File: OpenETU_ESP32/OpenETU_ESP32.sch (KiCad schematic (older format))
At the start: 2 parts

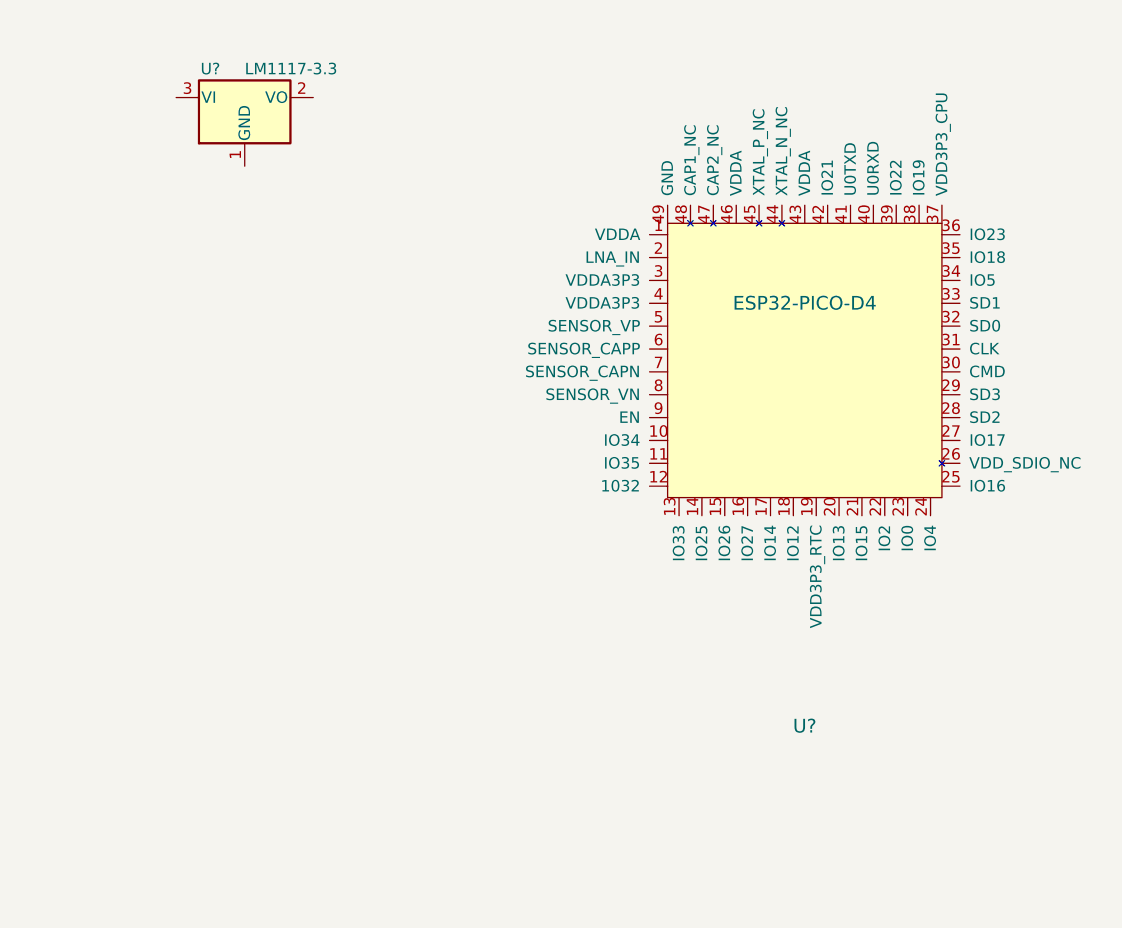
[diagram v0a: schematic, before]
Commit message: Changes
Started ramping up Schematic design for the esp32 vs of this board
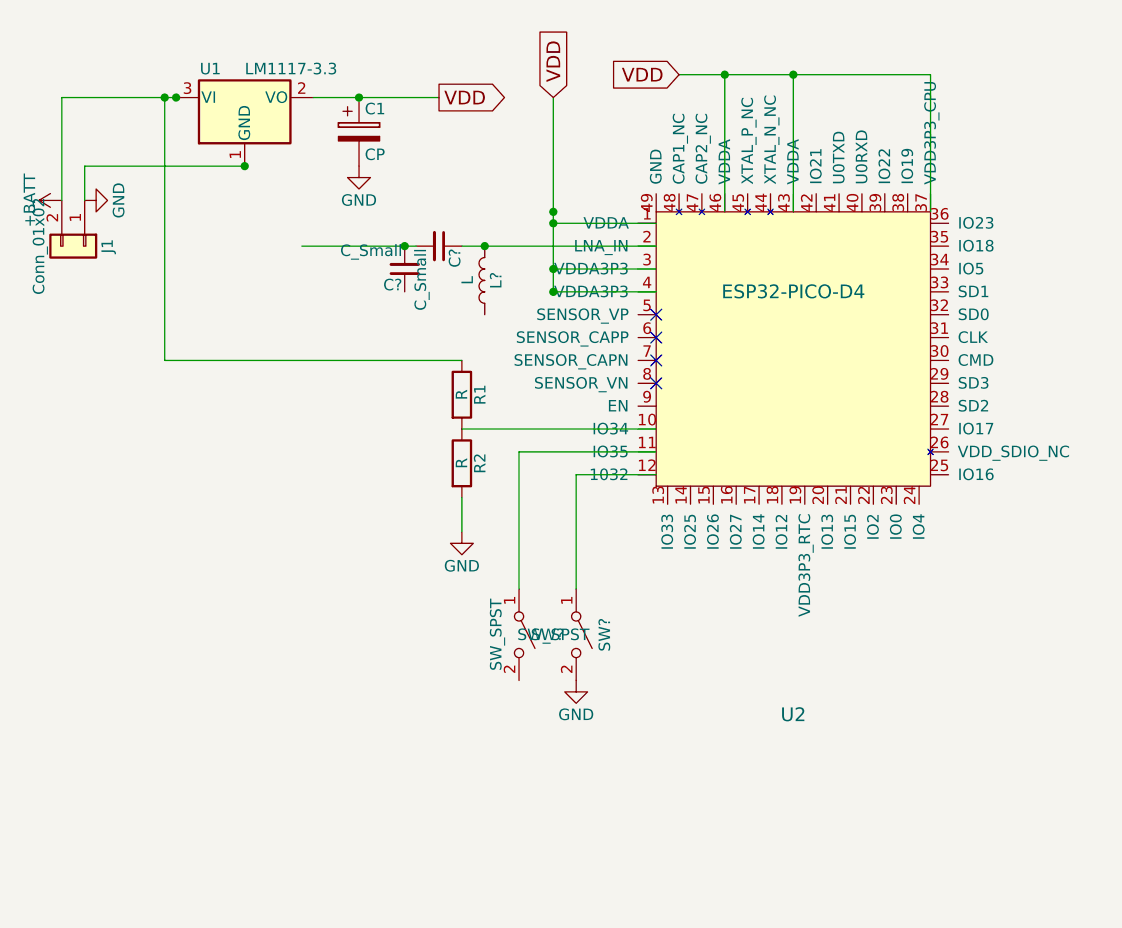
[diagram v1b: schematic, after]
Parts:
- added C1: CP, symbol CP
- added C? (x2): C_Small, symbol C_Small
- added J1: Conn_01x02, symbol Conn_01x02
- added L?: L, symbol L
- added R1, R2: R, symbol R
- added SW? (x2): SW_SPST, symbol SW_SPST
- gave numbers to parts that had none: 2
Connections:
- net labels added: +BATT, GND, VDD
- wire segments 0 -> 23
- no-connect marks 0 -> 4
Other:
- moved on the sheet: U2

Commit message: Just updating for the night
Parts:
- added C? (x2): C_Small, symbol C_Small
- added D?: LED, symbol LED
- added IC?: A1302KUA-T, symbol A1302KUA-T
- added R?: R_Small, symbol R_Small
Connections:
- wire segments 23 -> 31
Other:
- moved on the sheet: C?, L?
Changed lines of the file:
@@
 LIBS:valves
 LIBS:esp32-pico-d4
+LIBS:ETrigger-smaliffying-cache
 LIBS:OpenETU_ESP32-cache
 EELAYER 25 0
@@
 	1    0    0    -1
 $EndComp
-Wire Wire Line
-	3650 2850 4200 2850
 $Comp
 L GND #PWR01
@@
 	1    0    0    -1
 $EndComp
-Connection ~ 3850 2850
 Text GLabel 4200 2850 2    60   Output ~ 0
 VDD
-Wire Wire Line
-	5150 3400 4700 3400
-Wire Wire Line
-	4700 2850 4700 3700
-Wire Wire Line
-	4700 3700 5150 3700
-Connection ~ 4700 3400
-Wire Wire Line
-	5150 3600 4700 3600
-Connection ~ 4700 3600
 Text GLabel 4700 2850 1    60   Input ~ 0
 VDD
-Wire Wire Line
-	5450 3350 5450 2750
-Wire Wire Line
-	5250 2750 6350 2750
-Wire Wire Line
-	5750 2750 5750 3350
-Wire Wire Line
-	6350 2750 6350 3350
-Connection ~ 5750 2750
-Connection ~ 5450 2750
 Text GLabel 5250 2750 0    60   Input ~ 0
 VDD
@@
 NoConn ~ 5150 4000
 NoConn ~ 5150 4100
-Wire Wire Line
-	3050 2850 2550 2850
-Wire Wire Line
-	2550 2850 2550 3300
 $Comp
 L Conn_01x02 J1
@@
 	0    1    1    0
 $EndComp
-Wire Wire Line
-	3350 3150 2650 3150
-Wire Wire Line
-	2650 3150 2650 3300
-Connection ~ 3000 2850
 $Comp
 L R R1
@@
 	1    0    0    -1
 $EndComp
-Wire Wire Line
-	3000 2850 3000 4000
-Wire Wire Line
-	3000 4000 4300 4000
-Wire Wire Line
-	4300 4300 5150 4300
 $Comp
 L R R2
@@
 	1    0    0    -1
 $EndComp
-Wire Wire Line
-	4300 4600 4300 4750
 $Comp
 L GND #PWR02
@@
 	0    -1   -1   0
 $EndComp
-Connection ~ 3350 3150
-Connection ~ 4700 3700
-Connection ~ 4700 3350
-Connection ~ 3050 2850
-Wire Wire Line
-	4300 3500 5150 3500
 $Comp
 L L L?
 U 1 1 5A060289
-P 4400 3650
-F 0 "L?" V 4350 3650 50  0000 C CNN
-F 1 "L" V 4475 3650 50  0000 C CNN
-F 2 "" H 4400 3650 50  0001 C CNN
-F 3 "" H 4400 3650 50  0001 C CNN
-	1    4400 3650
-	-1   0    0    1
+P 4250 3500
+F 0 "L?" V 4200 3500 50  0000 C CNN
+F 1 "L" V 4325 3500 50  0000 C CNN
+F 2 "" H 4250 3500 50  0001 C CNN
+F 3 "" H 4250 3500 50  0001 C CNN
+	1    4250 3500
+	0    -1   -1   0
 $EndComp
 $Comp
 L C_Small C?
 U 1 1 5A06032C
-P 4200 3500
-F 0 "C?" H 4210 3570 50  0000 L CNN
-F 1 "C_Small" H 4210 3420 50  0000 L CNN
-F 2 "" H 4200 3500 50  0001 C CNN
-F 3 "" H 4200 3500 50  0001 C CNN
-	1    4200 3500
-	0    1    1    0
-$EndComp
-Connection ~ 4400 3500
+P 4450 3600
+F 0 "C?" H 4460 3670 50  0000 L CNN
+F 1 "C_Small" H 4460 3520 50  0000 L CNN
+F 2 "" H 4450 3600 50  0001 C CNN
+F 3 "" H 4450 3600 50  0001 C CNN
+	1    4450 3600
+	-1   0    0    1
+$EndComp
 $Comp
 L C_Small C?
@@
 	-1   0    0    1
 $EndComp
-Wire Wire Line
-	3600 3500 4100 3500
-Connection ~ 4050 3500
-Wire Wire Line
-	5150 4400 4550 4400
-Wire Wire Line
-	4550 4400 4550 5000
 $Comp
 L SW_SPST SW?
@@
 	0    1    1    0
 $EndComp
-Wire Wire Line
-	5150 4500 4800 4500
-Wire Wire Line
-	4800 4500 4800 5000
 $Comp
 L GND #PWR?
@@
 	1    0    0    -1
 $EndComp
+$Comp
+L A1302KUA-T IC?
+U 1 1 5A067DC6
+P 5200 6100
+F 0 "IC?" H 5200 6550 50  0000 L CNN
+F 1 "A1302KUA-T" H 5200 6450 50  0000 L CNN
+F 2 "" H 5200 5750 50  0000 L CIN
+F 3 "" H 5100 6100 50  0000 C CNN
+	1    5200 6100
+	0    -1   -1   0
+$EndComp
+$Comp
+L R_Small R?
+U 1 1 5A06832A
+P 4100 3000
+F 0 "R?" H 4130 3020 50  0000 L CNN
+F 1 "R_Small" H 4130 2960 50  0000 L CNN
+F 2 "" H 4100 3000 50  0001 C CNN
+F 3 "" H 4100 3000 50  0001 C CNN
+	1    4100 3000
+	1    0    0    -1
+$EndComp
+$Comp
+L LED D?
+U 1 1 5A0683C3
+P 4100 3250
+F 0 "D?" H 4100 3350 50  0000 C CNN
+F 1 "LED" H 4100 3150 50  0000 C CNN
+F 2 "" H 4100 3250 50  0001 C CNN
+F 3 "" H 4100 3250 50  0001 C CNN
+	1    4100 3250
+	0    -1   -1   0
+$EndComp
+$Comp
+L GND #PWR?
+U 1 1 5A068443
+P 4100 3400
+F 0 "#PWR?" H 4100 3150 50  0001 C CNN
+F 1 "GND" H 4100 3250 50  0000 C CNN
+F 2 "" H 4100 3400 50  0001 C CNN
+F 3 "" H 4100 3400 50  0001 C CNN
+	1    4100 3400
+	0    1    1    0
+$EndComp
+$Comp
+L GND #PWR?
+U 1 1 5A068CD8
+P 5800 6200
+F 0 "#PWR?" H 5800 5950 50  0001 C CNN
+F 1 "GND" H 5800 6050 50  0000 C CNN
+F 2 "" H 5800 6200 50  0001 C CNN
+F 3 "" H 5800 6200 50  0001 C CNN
+	1    5800 6200
+	1    0    0    -1
+$EndComp
+$Comp
+L GND #PWR?
+U 1 1 5A069779
+P 4050 3700
+F 0 "#PWR?" H 4050 3450 50  0001 C CNN
+F 1 "GND" H 4050 3550 50  0000 C CNN
+F 2 "" H 4050 3700 50  0001 C CNN
+F 3 "" H 4050 3700 50  0001 C CNN
+	1    4050 3700
+	1    0    0    -1
+$EndComp
+$Comp
+L GND #PWR?
+U 1 1 5A0697AE
+P 4450 3700
+F 0 "#PWR?" H 4450 3450 50  0001 C CNN
+F 1 "GND" H 4450 3550 50  0000 C CNN
+F 2 "" H 4450 3700 50  0001 C CNN
+F 3 "" H 4450 3700 50  0001 C CNN
+	1    4450 3700
+	1    0    0    -1
+$EndComp
+Wire Wire Line
+	3650 2850 4200 2850
+Connection ~ 3850 2850
+Wire Wire Line
+	5150 3400 4700 3400
+Wire Wire Line
+	4150 3700 5150 3700
+Connection ~ 4700 3400
+Wire Wire Line
+	5150 3600 4700 3600
+Connection ~ 4700 3600
+Wire Wire Line
+	5450 3350 5450 2750
+Wire Wire Line
+	5250 2750 6350 2750
+Wire Wire Line
+	5750 2750 5750 3350
+Wire Wire Line
+	6350 2750 6350 3350
+Connection ~ 5750 2750
+Connection ~ 5450 2750
+Wire Wire Line
+	3050 2850 2550 2850
+Wire Wire Line
+	2550 2850 2550 3300
+Wire Wire Line
+	3350 3150 2650 3150
+Wire Wire Line
+	2650 3150 2650 3300
+Connection ~ 3000 2850
+Wire Wire Line
+	3000 2850 3000 4000
+Wire Wire Line
+	3000 4000 4300 4000
+Wire Wire Line
+	4300 4300 5150 4300
+Wire Wire Line
+	4300 4600 4300 4750
+Connection ~ 3350 3150
+Connection ~ 4700 3700
+Connection ~ 3050 2850
+Wire Wire Line
+	3600 3500 4100 3500
+Connection ~ 4050 3500
+Wire Wire Line
+	5150 4400 4550 4400
+Wire Wire Line
+	4550 4400 4550 5000
+Wire Wire Line
+	5150 4500 4800 4500
+Wire Wire Line
+	4800 4500 4800 5000
+Wire Wire Line
+	5200 4550 5200 5800
+Wire Wire Line
+	4100 2850 4100 2900
+Connection ~ 4100 2850
+Wire Wire Line
+	4800 6200 3650 6200
+Wire Wire Line
+	3650 6200 3650 2850
+Wire Wire Line
+	5600 6200 5800 6200
+Wire Wire Line
+	5150 3500 4400 3500
+Connection ~ 4450 3500
+Wire Wire Line
+	4700 3400 4700 2850
+Wire Wire Line
+	4700 3600 4700 3700
+Wire Wire Line
+	4150 4250 4150 3700
+$Comp
+L C_Small C?
+U 1 1 5A06AB7D
+P 4150 4350
+F 0 "C?" H 4160 4420 50  0000 L CNN
+F 1 "C_Small" H 4160 4270 50  0000 L CNN
+F 2 "" H 4150 4350 50  0001 C CNN
+F 3 "" H 4150 4350 50  0001 C CNN
+	1    4150 4350
+	-1   0    0    1
+$EndComp
+$Comp
+L C_Small C?
+U 1 1 5A06ABD8
+P 3800 4350
+F 0 "C?" H 3810 4420 50  0000 L CNN
+F 1 "C_Small" H 3810 4270 50  0000 L CNN
+F 2 "" H 3800 4350 50  0001 C CNN
+F 3 "" H 3800 4350 50  0001 C CNN
+	1    3800 4350
+	-1   0    0    1
+$EndComp
+Wire Wire Line
+	3650 4250 4150 4250
+Connection ~ 3650 4250
+Connection ~ 3800 4250
+$Comp
+L GND #PWR?
+U 1 1 5A06AD2D
+P 3800 4450
+F 0 "#PWR?" H 3800 4200 50  0001 C CNN
+F 1 "GND" H 3800 4300 50  0000 C CNN
+F 2 "" H 3800 4450 50  0001 C CNN
+F 3 "" H 3800 4450 50  0001 C CNN
+	1    3800 4450
+	1    0    0    -1
+$EndComp
+$Comp
+L GND #PWR?
+U 1 1 5A06AD68
+P 4150 4450
+F 0 "#PWR?" H 4150 4200 50  0001 C CNN
+F 1 "GND" H 4150 4300 50  0000 C CNN
+F 2 "" H 4150 4450 50  0001 C CNN
+F 3 "" H 4150 4450 50  0001 C CNN
+	1    4150 4450
+	1    0    0    -1
+$EndComp
